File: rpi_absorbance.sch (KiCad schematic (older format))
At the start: 34 parts, among them CON1 BARREL_JACK, P1 CONN_02X08, P2 CONN_01X02, P3 RPI_HEADER, P4 STEPPER_CONN, Q1 ZTX692B, U1 R-78B5.0-1.5L, U2 MUN5216DW1T1G, U3 DRV8825, U4 TCA9406DCUR

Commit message: Update layout
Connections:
- wire segments 114 -> 113
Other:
- moved on the sheet: RV1
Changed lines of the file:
@@
 Text Label 7350 4650 0    60   ~ 0
 V3P3
-Text Label 5850 4500 2    60   ~ 0
+Text Label 5850 4850 3    60   ~ 0
 V3P3
 $Comp
 L POT RV1
 U 1 1 56CD04D7
-P 5850 4650
-F 0 "RV1" H 5850 4570 50  0000 C CNN
-F 1 "POT" H 5850 4650 50  0000 C CNN
-F 2 "footprints:BOURNS_3362P" H 5850 4650 50  0001 C CNN
-F 3 "" H 5850 4650 50  0000 C CNN
-	1    5850 4650
+P 5850 4700
+F 0 "RV1" H 5850 4620 50  0000 C CNN
+F 1 "POT" H 5850 4700 50  0000 C CNN
+F 2 "footprints:BOURNS_3362P" H 5850 4700 50  0001 C CNN
+F 3 "" H 5850 4700 50  0000 C CNN
+	1    5850 4700
 	0    1    1    0
 $EndComp
@@
 L GND #PWR038
 U 1 1 56CD0763
-P 5850 4850
-F 0 "#PWR038" H 5850 4600 50  0001 C CNN
-F 1 "GND" H 5850 4700 50  0000 C CNN
-F 2 "" H 5850 4850 50  0000 C CNN
-F 3 "" H 5850 4850 50  0000 C CNN
-	1    5850 4850
-	1    0    0    -1
+P 5850 4550
+F 0 "#PWR038" H 5850 4300 50  0001 C CNN
+F 1 "GND" H 5850 4400 50  0000 C CNN
+F 2 "" H 5850 4550 50  0000 C CNN
+F 3 "" H 5850 4550 50  0000 C CNN
+	1    5850 4550
+	-1   0    0    1
 $EndComp
 Text Label 7350 3550 0    60   ~ 0
@@
 	0    1    1    0
 $EndComp
-Text Label 5250 6350 2    60   ~ 0
+Text Label 5250 6650 3    60   ~ 0
 PERI
 $Comp
@@
 L GND #PWR053
 U 1 1 56D3711B
-P 5250 6650
-F 0 "#PWR053" H 5250 6400 50  0001 C CNN
-F 1 "GND" H 5250 6500 50  0000 C CNN
-F 2 "" H 5250 6650 50  0000 C CNN
-F 3 "" H 5250 6650 50  0000 C CNN
-	1    5250 6650
-	1    0    0    -1
+P 5250 6350
+F 0 "#PWR053" H 5250 6100 50  0001 C CNN
+F 1 "GND" H 5250 6200 50  0000 C CNN
+F 2 "" H 5250 6350 50  0000 C CNN
+F 3 "" H 5250 6350 50  0000 C CNN
+	1    5250 6350
+	-1   0    0    1
 $EndComp
 Text Notes 1200 2800 0    60   ~ 0
@@
 	7350 4700 7350 4650
 Wire Wire Line
-	5850 4850 5850 4800
-Wire Wire Line
 	6050 4550 6150 4550
 Wire Wire Line
-	6050 4650 6050 4550
-Wire Wire Line
-	6000 4650 6050 4650
+	6050 4700 6050 4550
+Wire Wire Line
+	6000 4700 6050 4700
 Wire Wire Line
 	7350 3300 7350 3350

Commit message: Complete stepper driver circuit
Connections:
- net labels removed: GPIO11
- no-connect marks 4 -> 5
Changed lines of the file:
@@
 	1    0    0    -1
 $EndComp
+Text Label 4200 6350 0    60   ~ 0
+MODE2
+Text Label 4200 6450 0    60   ~ 0
+MODE1
 Text Label 3100 6650 2    60   ~ 0
-MODE2
+MODE0
+Text Label 4200 6750 0    60   ~ 0
+STEP
 Text Label 3100 6750 2    60   ~ 0
-MODE1
+nENBL
 Text Label 3100 6850 2    60   ~ 0
-MODE0
+DIR
+Text Label 4200 6950 0    60   ~ 0
+DECAY
 Text Label 3100 6950 2    60   ~ 0
-STEP
+nFAULT
+Text Label 4200 7050 0    60   ~ 0
+nSLEEP
 Text Label 3100 7050 2    60   ~ 0
-nENBL
-Text Label 4200 7150 0    60   ~ 0
-DIR
-Text Label 4200 7050 0    60   ~ 0
-DECAY
-Text Label 4200 6950 0    60   ~ 0
-nFAULT
-Text Label 4200 6450 0    60   ~ 0
-nSLEEP
-Text Label 4200 6750 0    60   ~ 0
 nRESET
 Text Label 3100 5850 2    60   ~ 0
@@
 	1    0    0    -1
 $EndComp
-Text Label 4200 6350 0    60   ~ 0
+Text Label 4200 7150 0    60   ~ 0
 PERI
 $Comp
@@
 Text Label 3100 6250 2    60   ~ 0
 GPIO9
-Text Label 3100 6350 2    60   ~ 0
-GPIO11
 Text Label 3600 4250 0    60   ~ 0
 GPIO10
 Text Label 3600 4350 0    60   ~ 0
 GPIO9
-Text Label 3600 4450 0    60   ~ 0
-GPIO11
 $Comp
 L MUN5216DW1T1G U2
@@
 Connection ~ 3800 3750
 Connection ~ 1800 2300
+Text Label 3100 6350 2    60   ~ 0
+nHOME
+NoConn ~ 3600 4450
 $EndSCHEMATC

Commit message: Reorganize pcb
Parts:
- added F?: F_Small, symbol F_Small
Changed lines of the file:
@@
 L +12V #PWR046
 U 1 1 56D24636
-P 2900 3500
-F 0 "#PWR046" H 2900 3350 50  0001 C CNN
-F 1 "+12V" H 2900 3640 50  0000 C CNN
-F 2 "" H 2900 3500 50  0000 C CNN
-F 3 "" H 2900 3500 50  0000 C CNN
-	1    2900 3500
+P 2900 3300
+F 0 "#PWR046" H 2900 3150 50  0001 C CNN
+F 1 "+12V" H 2900 3440 50  0000 C CNN
+F 2 "" H 2900 3300 50  0000 C CNN
+F 3 "" H 2900 3300 50  0000 C CNN
+	1    2900 3300
 	1    0    0    -1
 $EndComp
@@
 nHOME
 NoConn ~ 3600 4450
+$Comp
+L F_Small F?
+U 1 1 56D4E462
+P 2900 3400
+F 0 "F?" H 2860 3460 50  0000 L CNN
+F 1 "F_Small" H 2780 3340 50  0000 L CNN
+F 2 "" H 2900 3400 50  0000 C CNN
+F 3 "" H 2900 3400 50  0000 C CNN
+	1    2900 3400
+	0    1    1    0
+$EndComp
 $EndSCHEMATC

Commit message: Change potentiometer footprint
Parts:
- removed P1: CONN_02X08, Pin_Headers:Pin_Header_Straight_2x08, symbol CONN_02X08
- added P1, P5: CONN_02X04, Pin_Headers:Pin_Header_Straight_2x04, symbol CONN_02X04
- F1: renamed from F?; footprint (none) -> Discret:CP4
- RV1, RV2: footprint footprints:BOURNS_3362P -> footprints:BOURNS_TC33
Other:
- moved on the sheet: R10, R9
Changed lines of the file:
@@
 F 0 "RV1" H 5850 4620 50  0000 C CNN
 F 1 "POT" H 5850 4700 50  0000 C CNN
-F 2 "footprints:BOURNS_3362P" H 5850 4700 50  0001 C CNN
+F 2 "footprints:BOURNS_TC33" H 5850 4700 50  0001 C CNN
 F 3 "" H 5850 4700 50  0000 C CNN
 	1    5850 4700
@@
 	1    0    0    -1
 $EndComp
-Text Label 7750 3100 0    60   ~ 0
-V3P3
 Text Label 7850 3450 0    60   ~ 0
 nHOME
@@
 L +3.3V #PWR040
 U 1 1 56CD7200
-P 3050 4500
-F 0 "#PWR040" H 3050 4350 50  0001 C CNN
-F 1 "+3.3V" H 3050 4640 50  0000 C CNN
-F 2 "" H 3050 4500 50  0000 C CNN
-F 3 "" H 3050 4500 50  0000 C CNN
-	1    3050 4500
+P 3050 4550
+F 0 "#PWR040" H 3050 4400 50  0001 C CNN
+F 1 "+3.3V" H 3050 4690 50  0000 C CNN
+F 2 "" H 3050 4550 50  0000 C CNN
+F 3 "" H 3050 4550 50  0000 C CNN
+	1    3050 4550
 	-1   0    0    1
 $EndComp
-Text Label 1850 4250 2    60   ~ 0
+Text Label 1850 4300 2    60   ~ 0
 SWITCH1
-Text Label 1850 4350 2    60   ~ 0
+Text Label 1850 4400 2    60   ~ 0
 SWITCH2
 $Comp
@@
 L R_Small R9
 U 1 1 56CEBB96
-P 1900 4100
-F 0 "R9" H 1930 4120 50  0000 L CNN
-F 1 "10k" H 1930 4060 50  0000 L CNN
-F 2 "Resistors_SMD:R_0603" H 1900 4100 50  0001 C CNN
-F 3 "" H 1900 4100 50  0000 C CNN
-	1    1900 4100
+P 1900 4150
+F 0 "R9" H 1930 4170 50  0000 L CNN
+F 1 "10k" H 1930 4110 50  0000 L CNN
+F 2 "Resistors_SMD:R_0603" H 1900 4150 50  0001 C CNN
+F 3 "" H 1900 4150 50  0000 C CNN
+	1    1900 4150
 	1    0    0    -1
 $EndComp
@@
 L GND #PWR041
 U 1 1 56CEBCE7
-P 1900 4000
-F 0 "#PWR041" H 1900 3750 50  0001 C CNN
-F 1 "GND" H 1900 3850 50  0000 C CNN
-F 2 "" H 1900 4000 50  0000 C CNN
-F 3 "" H 1900 4000 50  0000 C CNN
-	1    1900 4000
+P 1900 4050
+F 0 "#PWR041" H 1900 3800 50  0001 C CNN
+F 1 "GND" H 1900 3900 50  0000 C CNN
+F 2 "" H 1900 4050 50  0000 C CNN
+F 3 "" H 1900 4050 50  0000 C CNN
+	1    1900 4050
 	-1   0    0    1
 $EndComp
@@
 L R_Small R10
 U 1 1 56CED46B
-P 1900 4500
-F 0 "R10" H 1930 4520 50  0000 L CNN
-F 1 "10k" H 1930 4460 50  0000 L CNN
-F 2 "Resistors_SMD:R_0603" H 1900 4500 50  0001 C CNN
-F 3 "" H 1900 4500 50  0000 C CNN
-	1    1900 4500
+P 1900 4550
+F 0 "R10" H 1930 4570 50  0000 L CNN
+F 1 "10k" H 1930 4510 50  0000 L CNN
+F 2 "Resistors_SMD:R_0603" H 1900 4550 50  0001 C CNN
+F 3 "" H 1900 4550 50  0000 C CNN
+	1    1900 4550
 	1    0    0    -1
 $EndComp
@@
 L GND #PWR042
 U 1 1 56CED57B
-P 1900 4600
-F 0 "#PWR042" H 1900 4350 50  0001 C CNN
-F 1 "GND" H 1900 4450 50  0000 C CNN
-F 2 "" H 1900 4600 50  0000 C CNN
-F 3 "" H 1900 4600 50  0000 C CNN
-	1    1900 4600
+P 1900 4650
+F 0 "#PWR042" H 1900 4400 50  0001 C CNN
+F 1 "GND" H 1900 4500 50  0000 C CNN
+F 2 "" H 1900 4650 50  0000 C CNN
+F 3 "" H 1900 4650 50  0000 C CNN
+	1    1900 4650
 	1    0    0    -1
 $EndComp
@@
 	-1   0    0    1
 $EndComp
-$Comp
-L CONN_02X08 P1
-U 1 1 56D2A790
-P 3350 4100
-F 0 "P1" H 3350 4550 50  0000 C CNN
-F 1 "CONN_02X08" V 3350 4100 50  0000 C CNN
-F 2 "Pin_Headers:Pin_Header_Straight_2x08" H 3350 2900 50  0001 C CNN
-F 3 "" H 3350 2900 50  0000 C CNN
-	1    3350 4100
-	1    0    0    -1
-$EndComp
 Text Label 1400 3400 2    60   ~ 0
 LED1
@@
 L GND #PWR049
 U 1 1 56D2C382
-P 3050 4150
-F 0 "#PWR049" H 3050 3900 50  0001 C CNN
-F 1 "GND" H 3050 4000 50  0000 C CNN
-F 2 "" H 3050 4150 50  0000 C CNN
-F 3 "" H 3050 4150 50  0000 C CNN
-	1    3050 4150
+P 3050 4200
+F 0 "#PWR049" H 3050 3950 50  0001 C CNN
+F 1 "GND" H 3050 4050 50  0000 C CNN
+F 2 "" H 3050 4200 50  0000 C CNN
+F 3 "" H 3050 4200 50  0000 C CNN
+	1    3050 4200
 	0    1    1    0
 $EndComp
@@
 L GND #PWR050
 U 1 1 56D2C4A3
-P 3900 4150
-F 0 "#PWR050" H 3900 3900 50  0001 C CNN
-F 1 "GND" H 3900 4000 50  0000 C CNN
-F 2 "" H 3900 4150 50  0000 C CNN
-F 3 "" H 3900 4150 50  0000 C CNN
-	1    3900 4150
+P 3900 4200
+F 0 "#PWR050" H 3900 3950 50  0001 C CNN
+F 1 "GND" H 3900 4050 50  0000 C CNN
+F 2 "" H 3900 4200 50  0000 C CNN
+F 3 "" H 3900 4200 50  0000 C CNN
+	1    3900 4200
 	0    -1   -1   0
 $EndComp
@@
 Text Label 3100 6250 2    60   ~ 0
 GPIO9
-Text Label 3600 4250 0    60   ~ 0
+Text Label 3600 4300 0    60   ~ 0
 GPIO10
-Text Label 3600 4350 0    60   ~ 0
+Text Label 3600 4400 0    60   ~ 0
 GPIO9
 $Comp
@@
 F 0 "RV2" H 5250 6420 50  0000 C CNN
 F 1 "POT" H 5250 6500 50  0000 C CNN
-F 2 "footprints:BOURNS_3362P" H 5250 6500 50  0001 C CNN
+F 2 "footprints:BOURNS_TC33" H 5250 6500 50  0001 C CNN
 F 3 "" H 5250 6500 50  0000 C CNN
 	1    5250 6500
@@
 Wire Wire Line
 	3600 3500 3600 3750
-Connection ~ 1900 4250
-Wire Wire Line
-	1900 4200 1900 4250
-Connection ~ 1900 4350
-Wire Wire Line
-	1900 4400 1900 4350
+Connection ~ 1900 4300
+Wire Wire Line
+	1900 4250 1900 4300
+Connection ~ 1900 4400
+Wire Wire Line
+	1900 4450 1900 4400
 Wire Wire Line
 	6000 6750 6000 6700
@@
 	1100 1600 3350 1600
 Wire Wire Line
-	3050 4500 3050 4450
-Wire Wire Line
-	3050 4450 3100 4450
-Wire Wire Line
-	1850 4250 3100 4250
-Wire Wire Line
-	1850 4350 3100 4350
+	3050 4550 3050 4500
+Wire Wire Line
+	3050 4500 3100 4500
+Wire Wire Line
+	1850 4300 3100 4300
+Wire Wire Line
+	1850 4400 3100 4400
 Wire Wire Line
 	2900 3850 3100 3850
@@
 	2900 3500 2900 3850
 Wire Wire Line
-	3050 4150 3100 4150
-Wire Wire Line
-	3900 4150 3600 4150
+	3050 4200 3100 4200
+Wire Wire Line
+	3900 4200 3600 4200
 Wire Wire Line
 	3100 3950 2750 3950
@@
 Text Label 3100 6350 2    60   ~ 0
 nHOME
-NoConn ~ 3600 4450
-$Comp
-L F_Small F?
+NoConn ~ 3600 4500
+$Comp
+L F_Small F1
 U 1 1 56D4E462
 P 2900 3400
-F 0 "F?" H 2860 3460 50  0000 L CNN
+F 0 "F1" H 2860 3460 50  0000 L CNN
 F 1 "F_Small" H 2780 3340 50  0000 L CNN
-F 2 "" H 2900 3400 50  0000 C CNN
+F 2 "Discret:CP4" H 2900 3400 50  0001 C CNN
 F 3 "" H 2900 3400 50  0000 C CNN
 	1    2900 3400
 	0    1    1    0
 $EndComp
+$Comp
+L CONN_02X04 P1
+U 1 1 56D4EA2B
+P 3350 3900
+F 0 "P1" H 3350 4150 50  0000 C CNN
+F 1 "CONN_02X04" H 3350 4200 50  0000 C CNN
+F 2 "Pin_Headers:Pin_Header_Straight_2x04" H 3350 2700 50  0001 C CNN
+F 3 "" H 3350 2700 50  0000 C CNN
+	1    3350 3900
+	1    0    0    -1
+$EndComp
+$Comp
+L CONN_02X04 P5
+U 1 1 56D4ED6E
+P 3350 4350
+F 0 "P5" H 3350 4000 50  0000 C CNN
+F 1 "CONN_02X04" H 3350 4100 50  0000 C CNN
+F 2 "Pin_Headers:Pin_Header_Straight_2x04" H 3350 3150 50  0001 C CNN
+F 3 "" H 3350 3150 50  0000 C CNN
+	1    3350 4350
+	1    0    0    -1
+$EndComp
+$Comp
+L +3.3V #PWR054
+U 1 1 56D4F704
+P 7750 3100
+F 0 "#PWR054" H 7750 2950 50  0001 C CNN
+F 1 "+3.3V" H 7750 3240 50  0000 C CNN
+F 2 "" H 7750 3100 50  0000 C CNN
+F 3 "" H 7750 3100 50  0000 C CNN
+	1    7750 3100
+	1    0    0    -1
+$EndComp
 $EndSCHEMATC

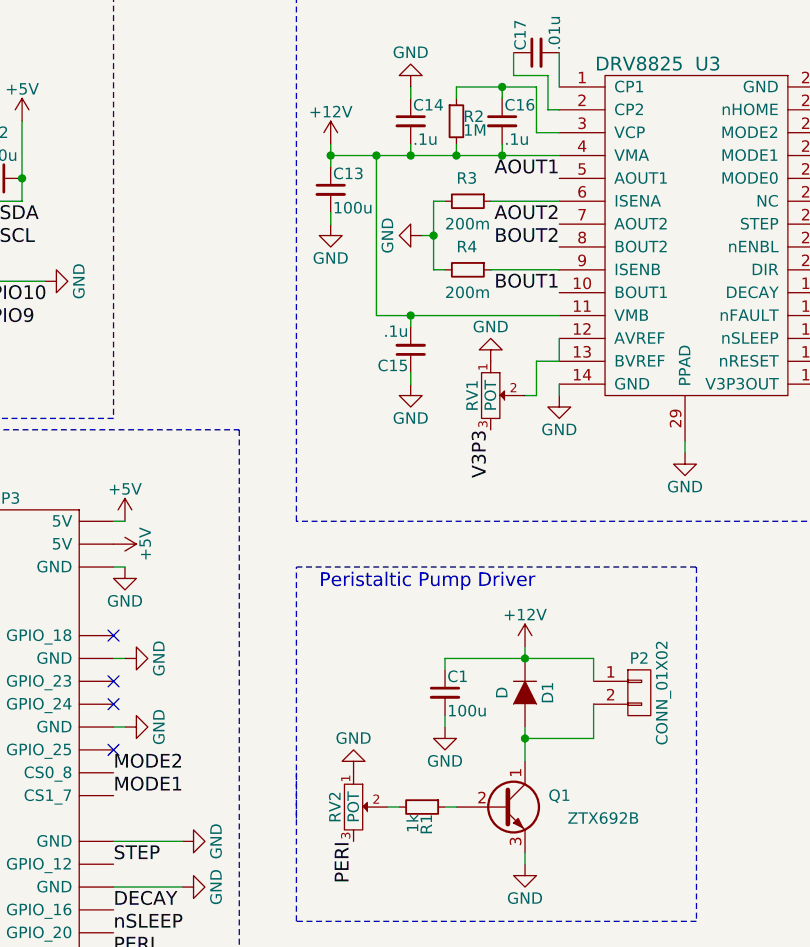
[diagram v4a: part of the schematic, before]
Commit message: Improve pcb layout, change capacitor footprints
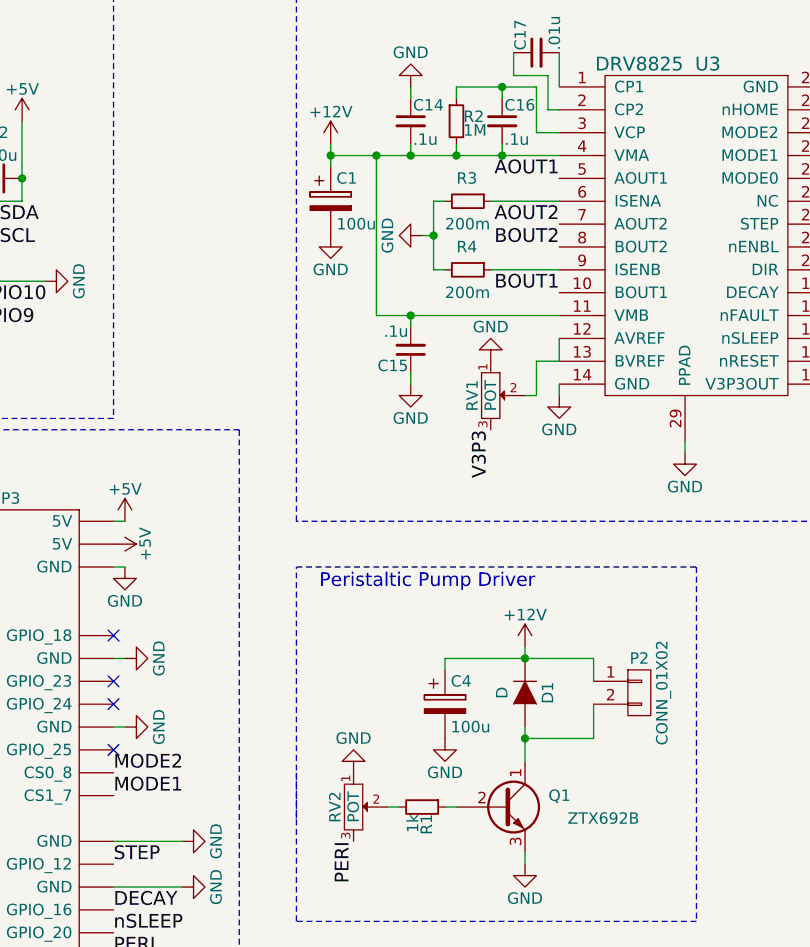
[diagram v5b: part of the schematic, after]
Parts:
- removed C1, C13: 100u, Capacitors_ThroughHole:C_Rect_L4_W2.5_P2.5, symbol C_Small
- added C1, C4: 100u, Capacitors_ThroughHole:C_Radial_D6.3_L11.2_P2.5, symbol CP
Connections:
- net +12V: now also C1.1, C4.1
- net GND: now also C1.2, C4.2
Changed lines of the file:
@@
-$EndComp
-$Comp
-L C_Small C13
-U 1 1 56CCD9DE
-P 5150 3800
-F 0 "C13" H 5160 3870 50  0000 L CNN
-F 1 "100u" H 5160 3720 50  0000 L CNN
-F 2 "Capacitors_ThroughHole:C_Rect_L4_W2.5_P2.5" H 5150 3800 50  0001 C CNN
-F 3 "" H 5150 3800 50  0000 C CNN
-	1    5150 3800
-	1    0    0    -1
 $EndComp
 $Comp
 L GND #PWR032
 U 1 1 56CCDA4E
-P 5150 3950
-F 0 "#PWR032" H 5150 3700 50  0001 C CNN
-F 1 "GND" H 5150 3800 50  0000 C CNN
-F 2 "" H 5150 3950 50  0000 C CNN
-F 3 "" H 5150 3950 50  0000 C CNN
-	1    5150 3950
+P 5150 4000
+F 0 "#PWR032" H 5150 3750 50  0001 C CNN
+F 1 "GND" H 5150 3850 50  0000 C CNN
+F 2 "" H 5150 4000 50  0000 C CNN
+F 3 "" H 5150 4000 50  0000 C CNN
+	1    5150 4000
 	1    0    0    -1
 $EndComp
@@
 $EndComp
 $Comp
-L C_Small C1
-U 1 1 56CFEC02
-P 5650 6000
-F 0 "C1" H 5660 6070 50  0000 L CNN
-F 1 "100u" H 5660 5920 50  0000 L CNN
-F 2 "Capacitors_ThroughHole:C_Rect_L4_W2.5_P2.5" H 5650 6000 50  0001 C CNN
-F 3 "" H 5650 6000 50  0000 C CNN
-	1    5650 6000
-	1    0    0    -1
-$EndComp
-$Comp
 L R_Small R1
 U 1 1 56CFEE09
@@
 L GND #PWR043
 U 1 1 56D00D89
-P 5650 6150
-F 0 "#PWR043" H 5650 5900 50  0001 C CNN
-F 1 "GND" H 5650 6000 50  0000 C CNN
-F 2 "" H 5650 6150 50  0000 C CNN
-F 3 "" H 5650 6150 50  0000 C CNN
-	1    5650 6150
+P 5650 6200
+F 0 "#PWR043" H 5650 5950 50  0001 C CNN
+F 1 "GND" H 5650 6050 50  0000 C CNN
+F 2 "" H 5650 6200 50  0000 C CNN
+F 3 "" H 5650 6200 50  0000 C CNN
+	1    5650 6200
 	1    0    0    -1
 $EndComp
@@
 	5650 5900 5650 5850
 Wire Wire Line
-	5650 6150 5650 6100
-Wire Wire Line
 	5450 6500 5400 6500
 Wire Wire Line
@@
 Wire Wire Line
 	5150 3600 5150 3700
-Wire Wire Line
-	5150 3900 5150 3950
 Connection ~ 5700 3650
 Connection ~ 5900 3650
@@
 	1    0    0    -1
 $EndComp
+$Comp
+L CP C1
+U 1 1 56D52FDF
+P 5150 3850
+F 0 "C1" H 5175 3950 50  0000 L CNN
+F 1 "100u" H 5175 3750 50  0000 L CNN
+F 2 "Capacitors_ThroughHole:C_Radial_D6.3_L11.2_P2.5" H 5188 3700 50  0001 C CNN
+F 3 "" H 5150 3850 50  0000 C CNN
+	1    5150 3850
+	1    0    0    -1
+$EndComp
+$Comp
+L CP C4
+U 1 1 56D53512
+P 5650 6050
+F 0 "C4" H 5675 6150 50  0000 L CNN
+F 1 "100u" H 5675 5950 50  0000 L CNN
+F 2 "Capacitors_ThroughHole:C_Radial_D6.3_L11.2_P2.5" H 5688 5900 50  0001 C CNN
+F 3 "" H 5650 6050 50  0000 C CNN
+	1    5650 6050
+	1    0    0    -1
+$EndComp
